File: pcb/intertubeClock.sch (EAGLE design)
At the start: 4 parts, among them U1 HV5122PG

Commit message: -ADDED SINK DRIVER -ADDED GATES AND DIVIDERS -FIRST PASS AT LAYOUT
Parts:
- added C3: 1UF, rcl:C-USC0805
- added C4: 0.1UF, rcl:C-USC0805
- added JP10: (no value), pinhead:PINHD-1X5
- added JP2: HV, pinhead:PINHD-1X4
- added JP3: DIGIT2, pinhead:PINHD-2X5
- added JP4: DIGIT3, pinhead:PINHD-2X5
- added JP5: DIGIT4, pinhead:PINHD-2X5
- added JP6: DIGIT5, pinhead:PINHD-2X5
- added JP7: DIGIT6, pinhead:PINHD-2X5
- added JP8: DIGIT7, pinhead:PINHD-2X5
- added JP9: DIGIT8, pinhead:PINHD-2X5
- added Q1, Q10, Q11, Q12, Q13, Q14, Q15, Q16, Q2, Q3, Q4, Q5, Q6, Q7, Q8, Q9: BSA223SP, transistor-fet:BSA223SP
- added R1, R3: 37.4K, rcl:R-US_R2512
- added R10, R11, R12, R13, R6, R7, R8, R9: 10K, rcl:R-US_R2512
- added R14, R16, R18, R20, R22, R24, R26, R28, R30, R32, R34, R36, R38, R40, R42, R44: 5K, rcl:R-US_R2512
- added R15, R17, R19, R21, R23, R25, R27, R29, R31, R33, R35, R37, R39, R41, R43, R45: 195K, rcl:R-US_R2512
- added R2, R4: 12K, rcl:R-US_R2512
- added R5: 50K, rcl:R-US_R2512
- added U2: HV5122PG, intertubeClock:HV5122PG
- C1: value (none) -> 1UF
- C2: value (none) -> 0.1UF
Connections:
- removed net HVOUT1: U1.HVOUT1
- removed net HVOUT10: U1.HVOUT10
- removed net HVOUT11: U1.HVOUT11
- removed net HVOUT12: U1.HVOUT12
- removed net HVOUT13: U1.HVOUT13
- removed net HVOUT14: U1.HVOUT14
- removed net HVOUT15: U1.HVOUT15
- removed net HVOUT16: U1.HVOUT16
- removed net HVOUT17: U1.HVOUT17
- removed net HVOUT18: U1.HVOUT18
- removed net HVOUT19: U1.HVOUT19
- removed net HVOUT20: U1.HVOUT20
- removed net HVOUT21: U1.HVOUT21
- removed net HVOUT22: U1.HVOUT22
- removed net HVOUT23: U1.HVOUT23
- removed net HVOUT24: U1.HVOUT24
- removed net HVOUT25: U1.HVOUT25
- removed net HVOUT26: U1.HVOUT26
- removed net HVOUT27: U1.HVOUT27
- removed net HVOUT28: U1.HVOUT28
- removed net HVOUT29: U1.HVOUT29
- removed net HVOUT3: U1.HVOUT3
- removed net HVOUT30: U1.HVOUT30
- removed net HVOUT31: U1.HVOUT31
- removed net HVOUT32: U1.HVOUT32
- removed net HVOUT4: U1.HVOUT4
- removed net HVOUT5: U1.HVOUT5
- removed net HVOUT6: U1.HVOUT6
- removed net HVOUT7: U1.HVOUT7
- removed net HVOUT8: U1.HVOUT8
- removed net HVOUT9: U1.HVOUT9
- new net A1_DIG1: JP1.2, Q1.D
- new net A1_DIG2: JP3.2, Q3.D
- new net A1_DIG3: JP4.2, Q5.D
- new net A1_DIG4: JP5.2, Q7.D
- new net A1_DIG5: JP6.2, Q9.D
- new net A1_DIG6: JP7.2, Q11.D
- new net A1_DIG7: JP8.2, Q13.D
- new net A1_DIG8: JP9.2, Q15.D
- new net A1_SEL#_DIG1: R15.1
- new net A1_SEL#_DIG2: R19.1
- new net A1_SEL#_DIG3: R23.1
- new net A1_SEL#_DIG4: R27.1
- new net A1_SEL#_DIG5: R31.1
- new net A1_SEL#_DIG6: R35.1
- new net A1_SEL#_DIG7: R39.1
- new net A1_SEL#_DIG8: R43.1
- new net A2_DIG1: JP1.3, Q2.D
- new net A2_DIG2: JP3.3, Q4.D
- new net A2_DIG3: JP4.3, Q6.D
- new net A2_DIG4: JP5.3, Q8.D
- new net A2_DIG5: JP6.3, Q10.D
- new net A2_DIG6: JP7.3, Q12.D
- new net A2_DIG7: JP8.3, Q14.D
- new net A2_DIG8: JP9.3, Q16.D
- new net A2_SEL#_DIG1: R17.1
- new net A2_SEL#_DIG2: R21.1
- new net A2_SEL#_DIG3: R25.1
- new net A2_SEL#_DIG4: R29.1
- new net A2_SEL#_DIG5: R33.1
- new net A2_SEL#_DIG6: R37.1
- new net A2_SEL#_DIG7: R41.1
- new net A2_SEL#_DIG8: R45.1
- new net DATA_OUT1: U1.DATA_OUT, U2.DATA_IN
- new net HV_IN: JP2.2, JP2.3, R1.1, R3.1, R5.1
- new net HV_VBA: Q1.S, Q10.S, Q11.S, Q12.S, Q13.S, Q14.S, Q15.S, Q16.S, Q2.S, Q3.S, Q4.S, Q5.S, Q6.S, Q7.S, Q8.S, Q9.S, R14.2, R16.2, R18.2, R20.2, R22.2, R24.2, R26.2, R28.2, R30.2, R32.2, R34.2, R36.2, R38.2, R40.2, R42.2, R44.2, R5.2
- new net HV_VBA_OFF: R3.2, R4.2
- new net HV_VS: R1.2, R10.2, R11.2, R12.2, R13.2, R2.2, R6.2, R7.2, R8.2, R9.2
- new net K01_DIG1: JP1.6
- new net K01_DIG2: JP3.6
- new net K01_DIG3: JP4.6
- new net K01_DIG4: JP5.6
- new net K01_DIG5: JP6.6
- new net K01_DIG6: JP7.6
- new net K01_DIG7: JP8.6
- new net K01_DIG8: JP9.6
- new net K23_DIG1: JP1.7
- new net K23_DIG2: JP3.7
- new net K23_DIG3: JP4.7
- new net K23_DIG4: JP5.7
- new net K23_DIG5: JP6.7
- new net K23_DIG6: JP7.7
- new net K23_DIG7: JP8.7
- new net K23_DIG8: JP9.7
- new net K45_DIG1: JP1.8
- new net K45_DIG2: JP3.8
- new net K45_DIG3: JP4.8
- new net K45_DIG4: JP5.8
- new net K45_DIG5: JP6.8
- new net K45_DIG6: JP7.8
- new net K45_DIG7: JP8.8
- new net K45_DIG8: JP9.8
- new net K67_DIG1: JP1.9
- new net K67_DIG2: JP3.9
- new net K67_DIG3: JP4.9
- new net K67_DIG4: JP5.9
- new net K67_DIG5: JP6.9
- new net K67_DIG6: JP7.9
- new net K67_DIG7: JP8.9
- new net K67_DIG8: JP9.9
- new net K89_DIG1: JP1.10
- new net K89_DIG2: JP3.10
- new net K89_DIG3: JP4.10
- new net K89_DIG4: JP5.10
- new net K89_DIG5: JP6.10
- new net K89_DIG6: JP7.10
- new net K89_DIG7: JP8.10
- new net K89_DIG8: JP9.10
- new net N$1: Q1.G, R14.1, R15.2
- new net N$10: Q10.G, R32.1, R33.2
- new net N$11: Q11.G, R34.1, R35.2
- new net N$12: Q12.G, R36.1, R37.2
- new net N$13: Q13.G, R38.1, R39.2
- new net N$14: Q14.G, R40.1, R41.2
- new net N$15: Q15.G, R42.1, R43.2
- new net N$16: Q16.G, R44.1, R45.2
- new net N$2: Q2.G, R16.1, R17.2
- new net N$3: Q3.G, R18.1, R19.2
- new net N$4: Q4.G, R20.1, R21.2
- new net N$5: Q5.G, R22.1, R23.2
- new net N$6: Q6.G, R24.1, R25.2
- new net N$7: Q7.G, R26.1, R27.2
- new net N$8: Q8.G, R28.1, R29.2
- new net N$9: Q9.G, R30.1, R31.2
- new net S_DIG1: JP1.4, R6.1
- new net S_DIG2: JP3.4, R7.1
- new net S_DIG3: JP4.4, R8.1
- new net S_DIG4: JP5.4, R9.1
- new net S_DIG5: JP6.4, R10.1
- new net S_DIG6: JP7.4, R11.1
- new net S_DIG7: JP8.4, R12.1
- new net S_DIG8: JP9.4, R13.1
- net CLK: now also JP10.3, U2.CLK
- net DATA_IN: now also JP10.2
- net GND: now also C3.2, C4.2, JP1.1, JP1.5, JP10.1, JP2.1, JP2.4, JP3.1, JP3.5, JP4.1, JP4.5, JP5.1, JP5.5, JP6.1, JP6.5, JP7.1, JP7.5, JP8.1, JP8.5, JP9.1, JP9.5, R2.1, R4.1, U2.GND
- net OE: now also JP10.4, U2.OE
- net STR: now also JP10.5, U2.STR
- net VDD: now also C3.1, C4.1, U2.VDD
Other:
- note added: "2018.02.11"
- note added: "2018.02.16"
- note added: "ADDED SINK DRIVER FIRST PASS AT LAYOUT"
- note added: "ADDED SUPPLY DIVIDERS ADDED DIGIT CONNECTORS ADDED ANODE GATES"
- note added: "DIVIDER POWER DISSIPATED = ~1W"
- note added: "Divider dissipation = ~0.5W"
- note added: "POWER DISSIPATED = ~1W"
- note added: "Vba = ANODE VOLTAGE MIN 170V TO MAX 300V"
- note added: "Vba_off = ANODE OFF VOLTAGE MIN 85V TO MAX 115V"
- note added: "Vgs must not exceed -20v, 5K/195K yields -5v."
- note added: "Vs = SCREEN VOLTAGE MIN 40V TO MAX 80V"

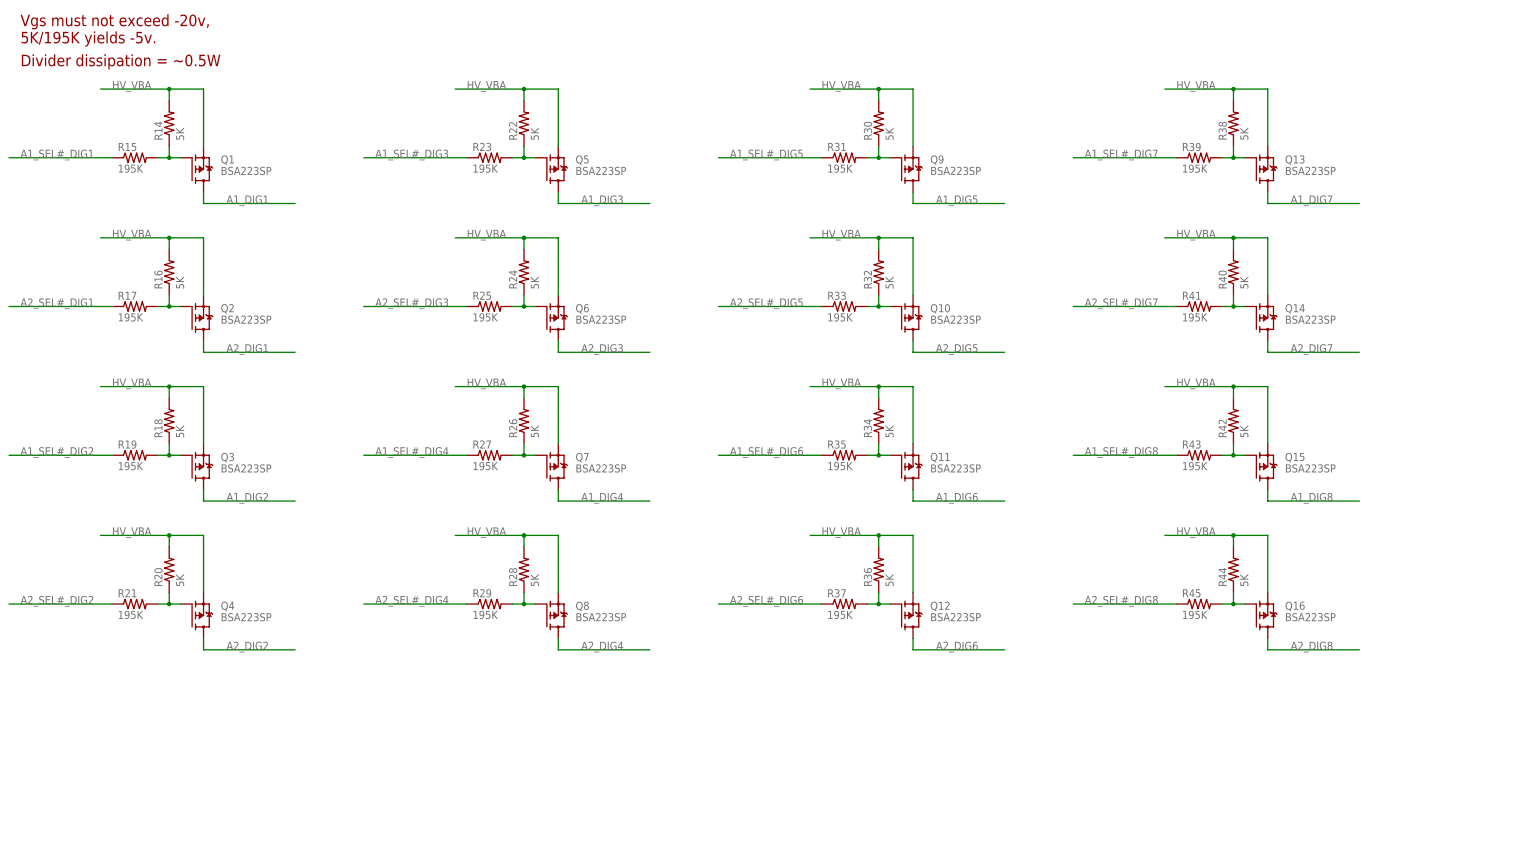
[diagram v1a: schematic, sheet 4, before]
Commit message: -Added power supply items. -Fixed anode nets. -Adjusted resistor packages.
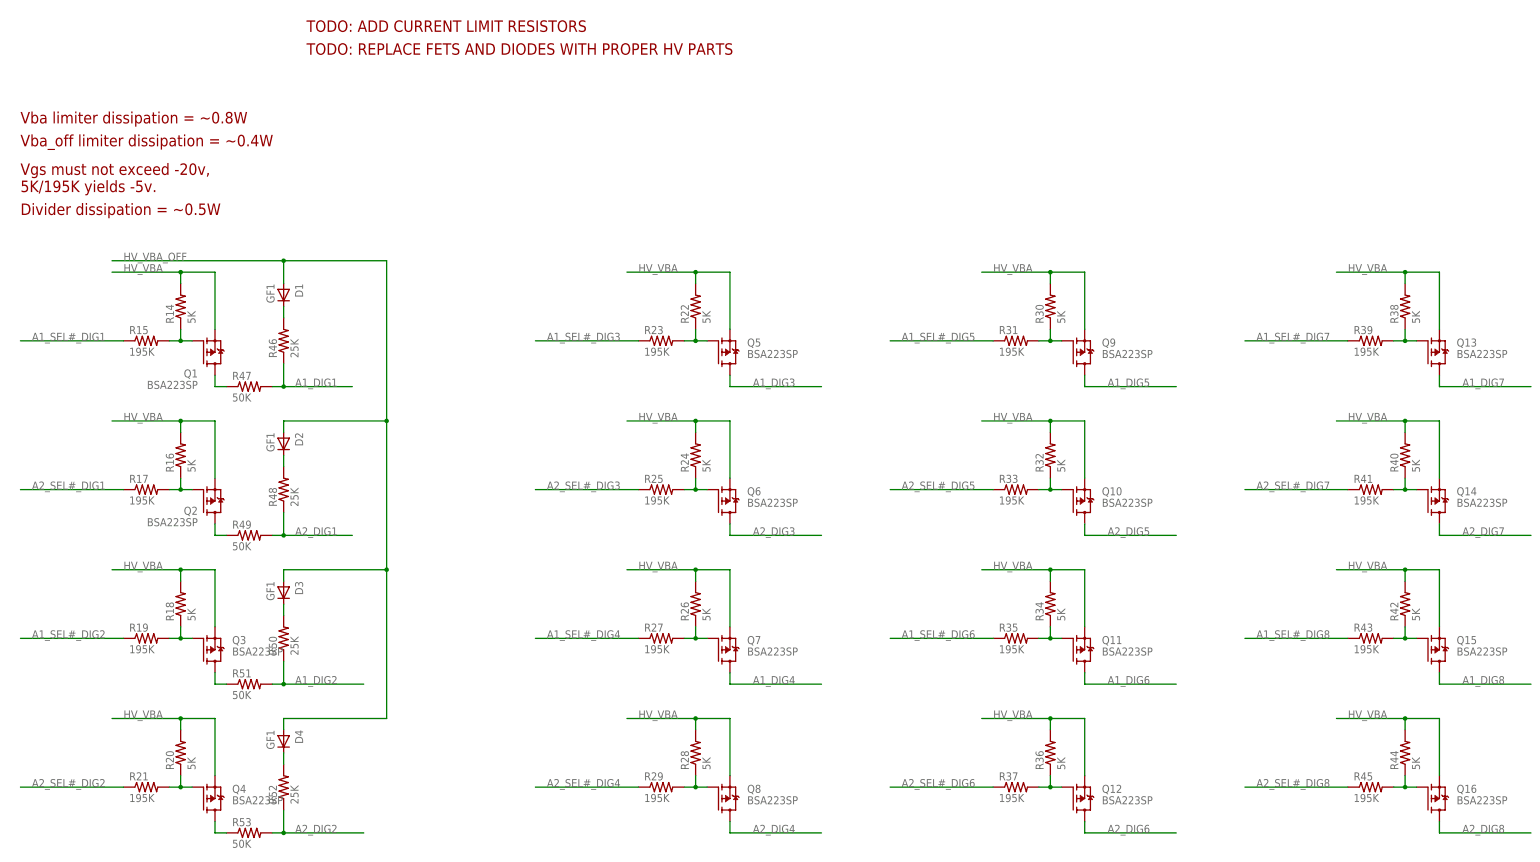
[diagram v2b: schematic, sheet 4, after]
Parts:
- added D1, D2, D3, D4: GF1, diode:GF1
- added R46, R48, R50, R52: 25K, rcl:R-US_R1206
- added R47, R49, R51, R53: 50K, rcl:R-US_R2010
- R1: value 37.4K -> 150K
- R14, R15, R16, R17, R18, R19, R20, R21: device rcl:R-US_R2512 -> rcl:R-US_R1206
- R2: value 12K -> 50K
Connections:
- new net HV_ENABLE: U2.HVOUT25
- new net N$17: Q1.D, R47.1
- new net N$18: D1.C, R46.2
- new net N$19: Q2.D, R49.1
- new net N$20: D2.C, R48.2
- new net N$21: Q3.D, R51.1
- new net N$22: D3.C, R50.2
- new net N$24: Q4.D, R53.1
- new net N$25: D4.C, R52.2
- net A1_DIG1: now also R46.1, R47.2; no longer Q1.D
- net A1_DIG2: now also R50.1, R51.2; no longer Q3.D
- net A1_SEL#_DIG1: now also U1.HVOUT1
- net A1_SEL#_DIG2: now also U1.HVOUT8
- net A1_SEL#_DIG3: now also U1.HVOUT15
- net A1_SEL#_DIG4: now also U1.HVOUT22
- net A1_SEL#_DIG5: now also U1.HVOUT29
- net A1_SEL#_DIG6: now also U2.HVOUT4
- net A1_SEL#_DIG7: now also U2.HVOUT11
- net A1_SEL#_DIG8: now also U2.HVOUT18
- net A2_DIG1: now also R48.1, R49.2; no longer Q2.D
- net A2_DIG2: now also R52.1, R53.2; no longer Q4.D
- net A2_SEL#_DIG1: now also U1.HVOUT2
- net A2_SEL#_DIG2: now also U1.HVOUT9
- net A2_SEL#_DIG3: now also U1.HVOUT16
- net A2_SEL#_DIG4: now also U1.HVOUT23
- net A2_SEL#_DIG5: now also U1.HVOUT30
- net A2_SEL#_DIG6: now also U2.HVOUT5
- net A2_SEL#_DIG7: now also U2.HVOUT12
- net A2_SEL#_DIG8: now also U2.HVOUT19
- net HV_VBA_OFF: now also D1.A, D2.A, D3.A, D4.A
- net K01_DIG1: now also U1.HVOUT3
- net K01_DIG2: now also U1.HVOUT10
- net K01_DIG3: now also U1.HVOUT17
- net K01_DIG4: now also U1.HVOUT24
- net K01_DIG5: now also U1.HVOUT31
- net K01_DIG6: now also U2.HVOUT6
- net K01_DIG7: now also U2.HVOUT13
- net K01_DIG8: now also U2.HVOUT20
- net K23_DIG1: now also U1.HVOUT4
- net K23_DIG2: now also U1.HVOUT11
- net K23_DIG3: now also U1.HVOUT18
- net K23_DIG4: now also U1.HVOUT25
- net K23_DIG5: now also U1.HVOUT32
- net K23_DIG6: now also U2.HVOUT7
- net K23_DIG7: now also U2.HVOUT14
- net K23_DIG8: now also U2.HVOUT21
- net K45_DIG1: now also U1.HVOUT5
- net K45_DIG2: now also U1.HVOUT12
- net K45_DIG3: now also U1.HVOUT19
- net K45_DIG4: now also U1.HVOUT26
- net K45_DIG5: now also U2.HVOUT1
- net K45_DIG6: now also U2.HVOUT8
- net K45_DIG7: now also U2.HVOUT15
- net K45_DIG8: now also U2.HVOUT22
- net K67_DIG1: now also U1.HVOUT6
- net K67_DIG2: now also U1.HVOUT13
- net K67_DIG3: now also U1.HVOUT20
- net K67_DIG4: now also U1.HVOUT27
- net K67_DIG5: now also U2.HVOUT2
- net K67_DIG6: now also U2.HVOUT9
- net K67_DIG7: now also U2.HVOUT16
- net K67_DIG8: now also U2.HVOUT23
- net K89_DIG1: now also U1.HVOUT7
- net K89_DIG2: now also U1.HVOUT14
- net K89_DIG3: now also U1.HVOUT21
- net K89_DIG4: now also U1.HVOUT28
- net K89_DIG5: now also U2.HVOUT3
- net K89_DIG6: now also U2.HVOUT10
- net K89_DIG7: now also U2.HVOUT17
- net K89_DIG8: now also U2.HVOUT24
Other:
- note added: "2018.02.18"
- note added: "FIXED VS DIVIDER VALUES"
- note added: "TODO: ADD CURRENT LIMIT RESISTORS"
- note added: "TODO: REPLACE FETS AND DIODES WITH PROPER HV PARTS"
- note added: "Vba limiter dissipation = ~0.8W"
- note added: "Vba_off limiter dissipation = ~0.4W"
- moved on the sheet: Q1, Q10, Q11, Q12, Q13, Q14, Q15, Q16, Q2, Q3, Q4, Q5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
